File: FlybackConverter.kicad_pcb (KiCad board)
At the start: 2 copper layers, 76.2 x 76.2 mm, 46 parts, among them J1 USB_C_Receptacle_PowerOnly_6P, T1 Transformer_1P_2S, U1 LNK6428K, U2 TPS25820DSST

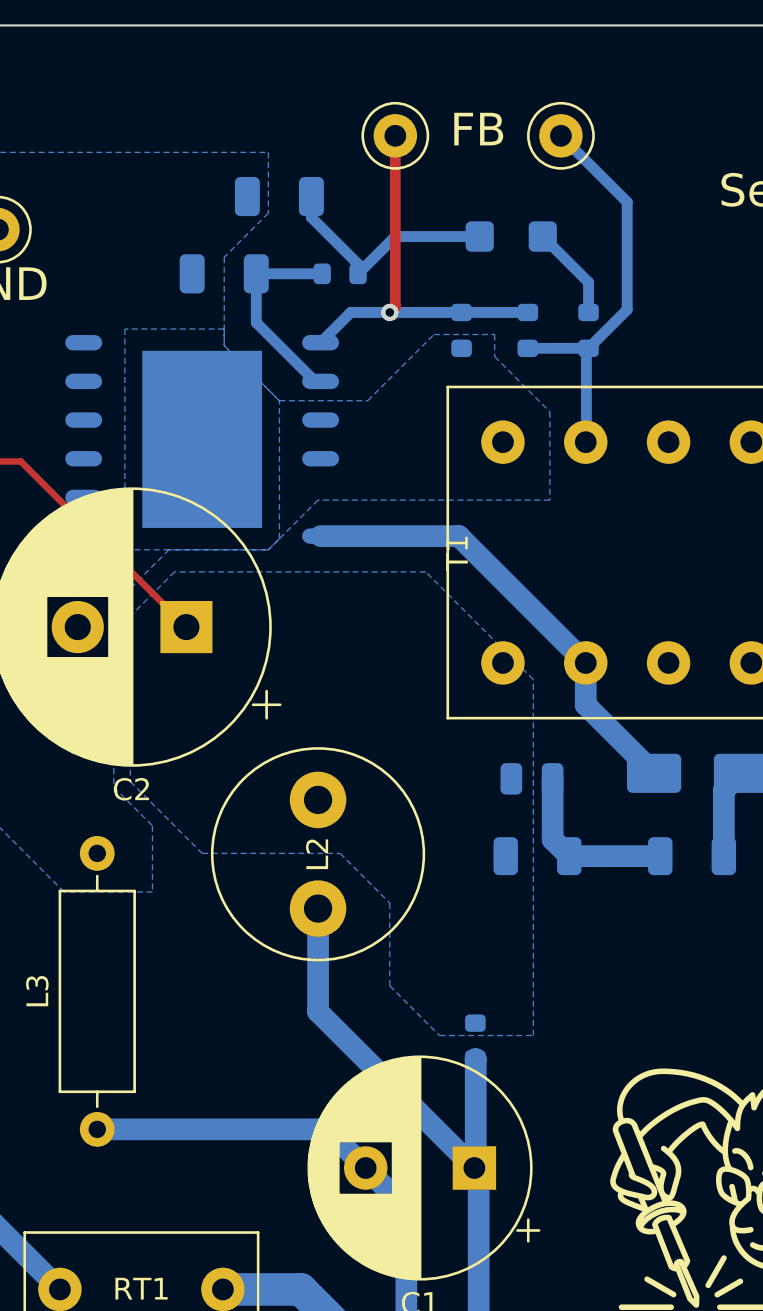
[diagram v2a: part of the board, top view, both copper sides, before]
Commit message: Net-(T1-AA)の塗りつぶし無し、配線に置き換え #8
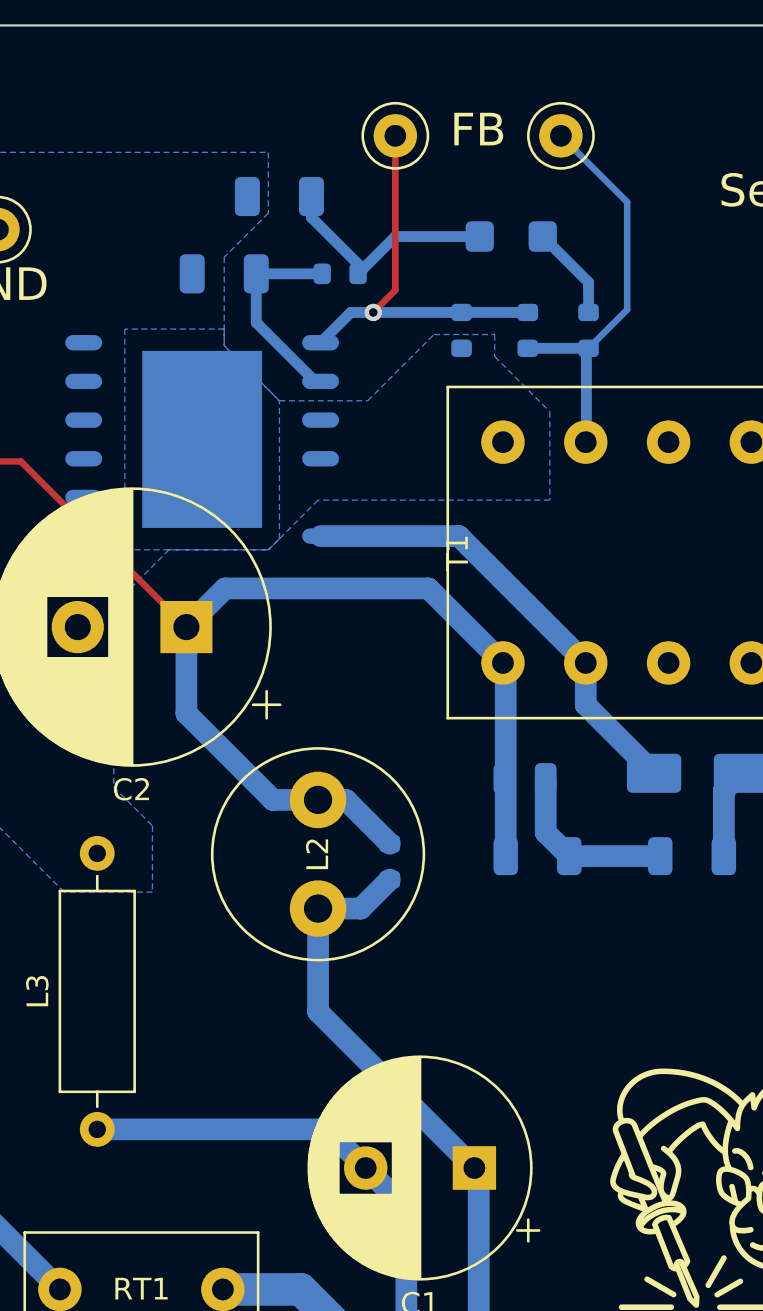
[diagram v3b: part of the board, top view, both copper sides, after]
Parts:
- moved R10 9.15 mm to (154.7, 89.3)
- moved C6 0.32 mm to (160.9, 85.5)
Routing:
- net Net-(T1-AA): track 16.7 -> 58.1 mm
- net Net-(BR1-+): track 27.8 -> 26.6 mm
- removed copper zone on B.Cu, net Net-(T1-AA)
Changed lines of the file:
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@@
   )
   (footprint "Resistor_SMD:R_0603_1608Metric" (layer "B.Cu")
-    (at 158.623 97.536 90)
+    (at 154.686 89.281 90)
     (descr "Resistor SMD 0603 (1608 Metric), square (rectangular) end terminal, IPC_7351 nominal, (Body size source: IPC-SM-782 page 72, https://www.pcb-3d.com/wordpress/wp-content/uploads/ipc-sm-782a_amendment_1_and_2.pdf), generated with kicad-footprint-generator")
     (tags "resistor")
@@
     (property "ki_keywords" "R res resistor")
     (attr smd)
-    (fp_text reference "R10" (at 1.524 -2.38 90) (layer "B.SilkS")
+    (fp_text reference "R10" (at 0 1.651 90) (layer "B.SilkS")
         (effects (font (size 1 1) (thickness 0.15)) (justify mirror))
     )
@@
   )
   (footprint "Capacitor_SMD:C_0805_2012Metric" (layer "B.Cu")
-    (at 161.2285 85.471)
+    (at 160.909 85.471)
     (descr "Capacitor SMD 0805 (2012 Metric), square (rectangular) end terminal, IPC_7351 nominal, (Body size source: IPC-SM-782 page 76, https://www.pcb-3d.com/wordpress/wp-content/uploads/ipc-sm-782a_amendment_1_and_2.pdf, https://docs.google.com/spreadsheets/d/1BsfQQcO9C6DZCsRaXUlFlo91Tg2WpOkGARC1WS5S8t0/edit?usp=sharing), generated with kicad-footprint-generator")
     (tags "capacitor")
@@
   (segment (start 151.384 91.44) (end 151.384 96.184323) (width 1) (layer "B.Cu") (net 1))
   (segment (start 151.384 96.184323) (end 158.577677 103.378) (width 1) (layer "B.Cu") (net 1))
+  (segment (start 153.352 91.44) (end 154.686 90.106) (width 1) (layer "B.Cu") (net 1))
   (segment (start 158.777 103.577323) (end 158.777 110.998) (width 1) (layer "B.Cu") (net 1))
   (segment (start 158.577677 103.378) (end 158.640677 103.441) (width 1) (layer "B.Cu") (net 1))
-  (segment (start 158.640677 98.378677) (end 158.623 98.361) (width 1) (layer "B.Cu") (net 1))
   (segment (start 158.577677 103.378) (end 158.777 103.577323) (width 1) (layer "B.Cu") (net 1))
-  (segment (start 158.640677 103.441) (end 158.640677 98.378677) (width 1) (layer "B.Cu") (net 1))
+  (segment (start 151.384 91.44) (end 153.352 91.44) (width 1) (layer "B.Cu") (net 1))
   (segment (start 151.799677 101.6) (end 153.577677 103.378) (width 1) (layer "B.Cu") (net 2))
   (segment (start 155.448 105.248323) (end 153.577677 103.378) (width 1) (layer "B.Cu") (net 2))
@@
   (segment (start 131.826 70.866) (end 137.705959 70.866) (width 0.3) (layer "F.Cu") (net 5))
   (segment (start 137.705959 70.866) (end 145.325959 78.486) (width 0.3) (layer "F.Cu") (net 5))
+  (segment (start 156.464 76.708) (end 159.893 80.137) (width 1) (layer "B.Cu") (net 5))
+  (segment (start 152.67 86.44) (end 154.686 88.456) (width 1) (layer "B.Cu") (net 5))
+  (segment (start 151.384 86.44) (end 149.305 86.44) (width 1) (layer "B.Cu") (net 5))
+  (segment (start 151.384 86.44) (end 152.67 86.44) (width 1) (layer "B.Cu") (net 5))
+  (segment (start 149.305 86.44) (end 145.325959 82.460959) (width 1) (layer "B.Cu") (net 5))
+  (segment (start 160.02 80.264) (end 160.02 89.027) (width 1) (layer "B.Cu") (net 5))
+  (segment (start 145.325959 78.486) (end 147.103959 76.708) (width 1) (layer "B.Cu") (net 5))
+  (segment (start 145.325959 82.460959) (end 145.325959 78.486) (width 1) (layer "B.Cu") (net 5))
+  (segment (start 159.893 80.137) (end 160.02 80.264) (width 1) (layer "B.Cu") (net 5))
+  (segment (start 147.103959 76.708) (end 156.464 76.708) (width 1) (layer "B.Cu") (net 5))
   (segment (start 195.596 62.722) (end 193.294 65.024) (width 1.5) (layer "B.Cu") (net 6))
   (segment (start 195.596 60.548) (end 195.596 62.722) (width 1.5) (layer "B.Cu") (net 6))
@@
   (segment (start 193.294 74.908) (end 193.294 65.024) (width 0.5) (layer "B.Cu") (net 6))
   (segment (start 193.696 60.548) (end 191.2405 60.548) (width 1.5) (layer "B.Cu") (net 7))
+  (segment (start 161.859 85.471) (end 161.859 87.941) (width 1) (layer "B.Cu") (net 8))
   (segment (start 162.945 89.027) (end 167.132 89.027) (width 1) (layer "B.Cu") (net 8))
-  (segment (start 162.1785 88.2605) (end 162.945 89.027) (width 1) (layer "B.Cu") (net 8))
-  (segment (start 162.1785 85.471) (end 162.1785 88.2605) (width 1) (layer "B.Cu") (net 8))
+  (segment (start 161.859 87.941) (end 162.945 89.027) (width 1) (layer "B.Cu") (net 8))
   (segment (start 151.575 62.23) (end 148.541 62.23) (width 0.5) (layer "B.Cu") (net 9))
   (segment (start 148.541 62.23) (end 148.541 64.475) (width 0.5) (layer "B.Cu") (net 9))
@@
   (segment (start 139.7 114.3) (end 142.24 116.84) (width 1) (layer "B.Cu") (net 14))
   (segment (start 134.62 114.3) (end 139.7 114.3) (width 1) (layer "B.Cu") (net 14))
-  (segment (start 154.94 63.754) (end 154.94 55.88) (width 0.5) (layer "F.Cu") (net 15))
-  (segment (start 154.686 64.008) (end 154.94 63.754) (width 0.5) (layer "F.Cu") (net 15))
-  (via (at 154.686 64.008) (size 0.8) (drill 0.4) (layers "F.Cu" "B.Cu") (net 15))
+  (segment (start 153.924 64.008) (end 154.94 62.992) (width 0.3) (layer "F.Cu") (net 15))
+  (segment (start 154.94 62.992) (end 154.94 55.88) (width 0.3) (layer "F.Cu") (net 15))
+  (via (at 153.924 64.008) (size 0.8) (drill 0.4) (layers "F.Cu" "B.Cu") (net 15))
+  (segment (start 153.924 64.008) (end 152.892 64.008) (width 0.5) (layer "B.Cu") (net 15))
   (segment (start 157.988 64.008) (end 161.036 64.008) (width 0.5) (layer "B.Cu") (net 15))
-  (segment (start 154.686 64.008) (end 157.988 64.008) (width 0.5) (layer "B.Cu") (net 15))
-  (segment (start 152.892 64.008) (end 154.686 64.008) (width 0.5) (layer "B.Cu") (net 15))
-  (segment (start 151.5 65.4) (end 152.892 64.008) (width 0.5) (layer "B.Cu") (net 15))
+  (segment (start 152.892 64.008) (end 151.5 65.4) (width 0.5) (layer "B.Cu") (net 15))
+  (segment (start 153.924 64.008) (end 157.988 64.008) (width 0.5) (layer "B.Cu") (net 15))
   (segment (start 134.62 104.08) (end 139.506 108.966) (width 1) (layer "B.Cu") (net 16))
   (segment (start 134.62 99.06) (end 134.62 104.08) (width 1) (layer "B.Cu") (net 16))
@@
   (segment (start 163.83 65.658) (end 163.733 65.755) (width 0.5) (layer "B.Cu") (net 20))
   (segment (start 163.733 65.755) (end 163.733 69.947) (width 0.5) (layer "B.Cu") (net 20))
-  (segment (start 165.608 58.928) (end 162.56 55.88) (width 0.5) (layer "B.Cu") (net 20))
-  (segment (start 163.83 65.658) (end 165.608 63.88) (width 0.5) (layer "B.Cu") (net 20))
-  (segment (start 165.608 63.88) (end 165.608 58.928) (width 0.5) (layer "B.Cu") (net 20))
+  (segment (start 165.608 58.928) (end 162.56 55.88) (width 0.3) (layer "B.Cu") (net 20))
+  (segment (start 163.83 65.658) (end 165.608 63.88) (width 0.3) (layer "B.Cu") (net 20))
+  (segment (start 165.608 63.88) (end 165.608 58.928) (width 0.3) (layer "B.Cu") (net 20))
   (segment (start 163.83 65.658) (end 161.036 65.658) (width 0.5) (layer "B.Cu") (net 20))
   (segment (start 196.41 92.134) (end 190.615 97.929) (width 0.3) (layer "B.Cu") (net 21))
@@
       )
     )
-  )
-  (zone (net 5) (net_name "Net-(T1-AA)") (layer "B.Cu") (hatch edge 0.5)
-    (priority 1)
-    (connect_pads (clearance 0.5))
-    (min_thickness 0.25) (filled_areas_thickness no)
-    (fill yes (thermal_gap 0.5) (thermal_bridge_width 0.5))
-    (polygon
-      (pts
-        (xy 142.748 77.978)
-        (xy 142.748 85.598)
-        (xy 146.05 88.9)
-        (xy 152.4 88.9)
-        (xy 154.686 91.186)
-        (xy 154.686 94.996)
-        (xy 156.972 97.282)
-        (xy 161.29 97.282)
-        (xy 161.29 80.899)
-        (xy 156.337 75.946)
-        (xy 144.78 75.946)
-      )
-    )

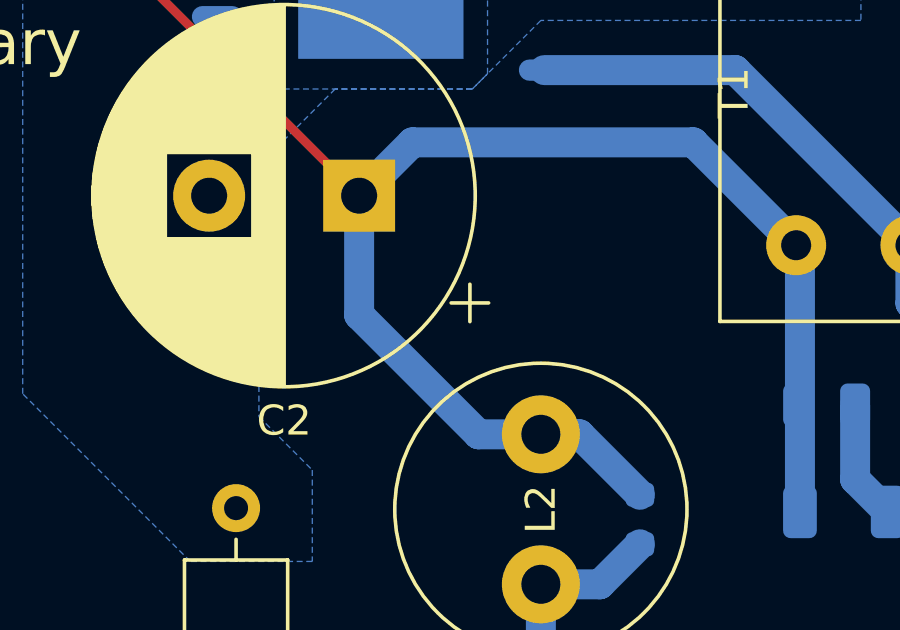
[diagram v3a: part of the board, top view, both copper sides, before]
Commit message: 配線位置微修正、DRC問題無し #8
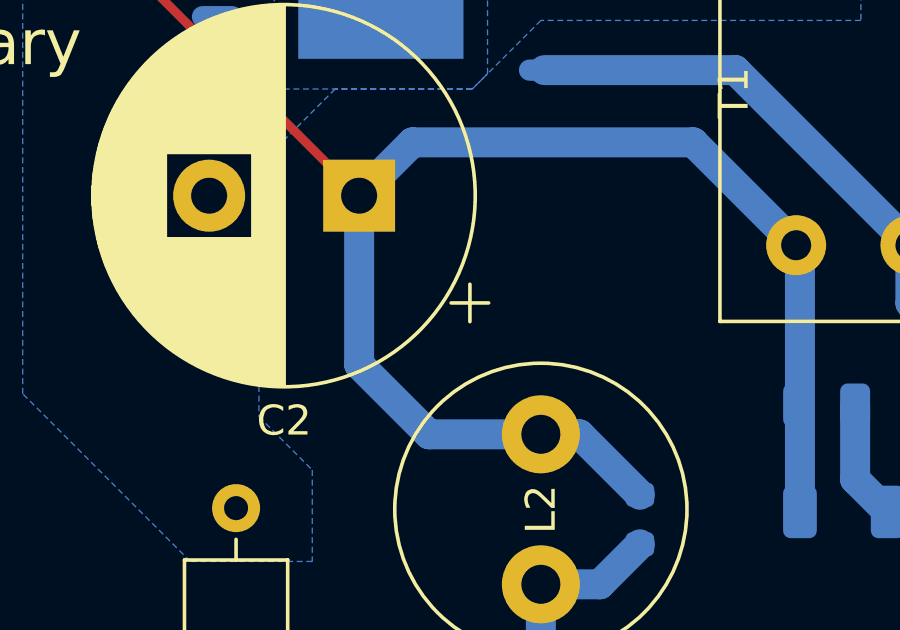
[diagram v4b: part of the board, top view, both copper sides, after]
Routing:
- net Net-(T1-AA): track 58.1 -> 59.1 mm
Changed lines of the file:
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@@
   (segment (start 156.464 76.708) (end 159.893 80.137) (width 1) (layer "B.Cu") (net 5))
   (segment (start 152.67 86.44) (end 154.686 88.456) (width 1) (layer "B.Cu") (net 5))
-  (segment (start 151.384 86.44) (end 149.305 86.44) (width 1) (layer "B.Cu") (net 5))
   (segment (start 151.384 86.44) (end 152.67 86.44) (width 1) (layer "B.Cu") (net 5))
-  (segment (start 149.305 86.44) (end 145.325959 82.460959) (width 1) (layer "B.Cu") (net 5))
+  (segment (start 151.384 86.44) (end 147.654 86.44) (width 1) (layer "B.Cu") (net 5))
   (segment (start 160.02 80.264) (end 160.02 89.027) (width 1) (layer "B.Cu") (net 5))
+  (segment (start 145.325959 84.111959) (end 145.325959 78.486) (width 1) (layer "B.Cu") (net 5))
   (segment (start 145.325959 78.486) (end 147.103959 76.708) (width 1) (layer "B.Cu") (net 5))
-  (segment (start 145.325959 82.460959) (end 145.325959 78.486) (width 1) (layer "B.Cu") (net 5))
+  (segment (start 147.654 86.44) (end 145.325959 84.111959) (width 1) (layer "B.Cu") (net 5))
   (segment (start 159.893 80.137) (end 160.02 80.264) (width 1) (layer "B.Cu") (net 5))
   (segment (start 147.103959 76.708) (end 156.464 76.708) (width 1) (layer "B.Cu") (net 5))
